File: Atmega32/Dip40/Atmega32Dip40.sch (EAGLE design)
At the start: 0 parts

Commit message: Add Atmega32 DIP40
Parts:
- added C1, C2: 100n, resistor:C-EUC1206
- added C10, C3: 22p, resistor:C-EUC1206
- added FTDI: 6H, adafruit:PINHD-1X6
- added IC1: MEGA32-P, atmel:MEGA32-P
- added L1: SMT, adafruit:LEDSMT1206
- added LED_ASP: BLUE_SMT, adafruit:LEDSMT1206
- added Q3: 16m, adafruit:CRYSTALHC49UP
- added R3: 330, resistor:R-EU_R1206
- added R4: 1k, resistor:R-EU_R1206
- added R5, R6: 10K, resistor:R-EU_0204/7
- added R7: 100K, resistor:R-EU_0204/7
- added X3: 057-010-1, con-panduit:057-010-1
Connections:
- new net DTR: C2.1, FTDI.1
- new net GND: C1.1, C10.1, C3.1, FTDI.6, IC1.GND, IC1.GND@1, L1.C, LED_ASP.C, X3-10.S, X3-3.S, X3-4.S, X3-6.S, X3-8.S
- new net LED_13: IC1.(OC1A)PD5, R3.1
- new net MISO: IC1.(MISO)PB6, X3-9.S
- new net MOSI: IC1.(MOSI)PB5, X3-1.S
- new net N$2: L1.A, R3.2
- new net N$3: LED_ASP.A, R4.2
- new net N$4: C1.2, IC1.AREF
- new net OX1: C10.2, IC1.XTAL2, Q3.2
- new net OX2: C3.2, IC1.XTAL1, Q3.1
- new net RESET: C2.2, FTDI.5, IC1.RESET, R7.1, X3-5.S
- new net RX: FTDI.2, IC1.(RXD)PD0
- new net SCK: IC1.(SCK)PB7, X3-7.S
- new net SCL: IC1.(SCL)PC0, R5.2
- new net SDA: IC1.(SDA)PC1, R6.2
- new net TX: FTDI.3, IC1.(TXD)PD1
- new net VCC: FTDI.4, IC1.AVCC, IC1.VCC, R4.1, R5.1, R6.1, R7.2, X3-2.S
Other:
- note added: "DTR"
- note added: "FTDI Serial"
- note added: "I2S Pull-UP"
- note added: "LED DIGITAL 13"
- note added: "Oscillator MCU"
- note added: "RESET"
- note added: "RX"
- note added: "SPI"
- note added: "TX"

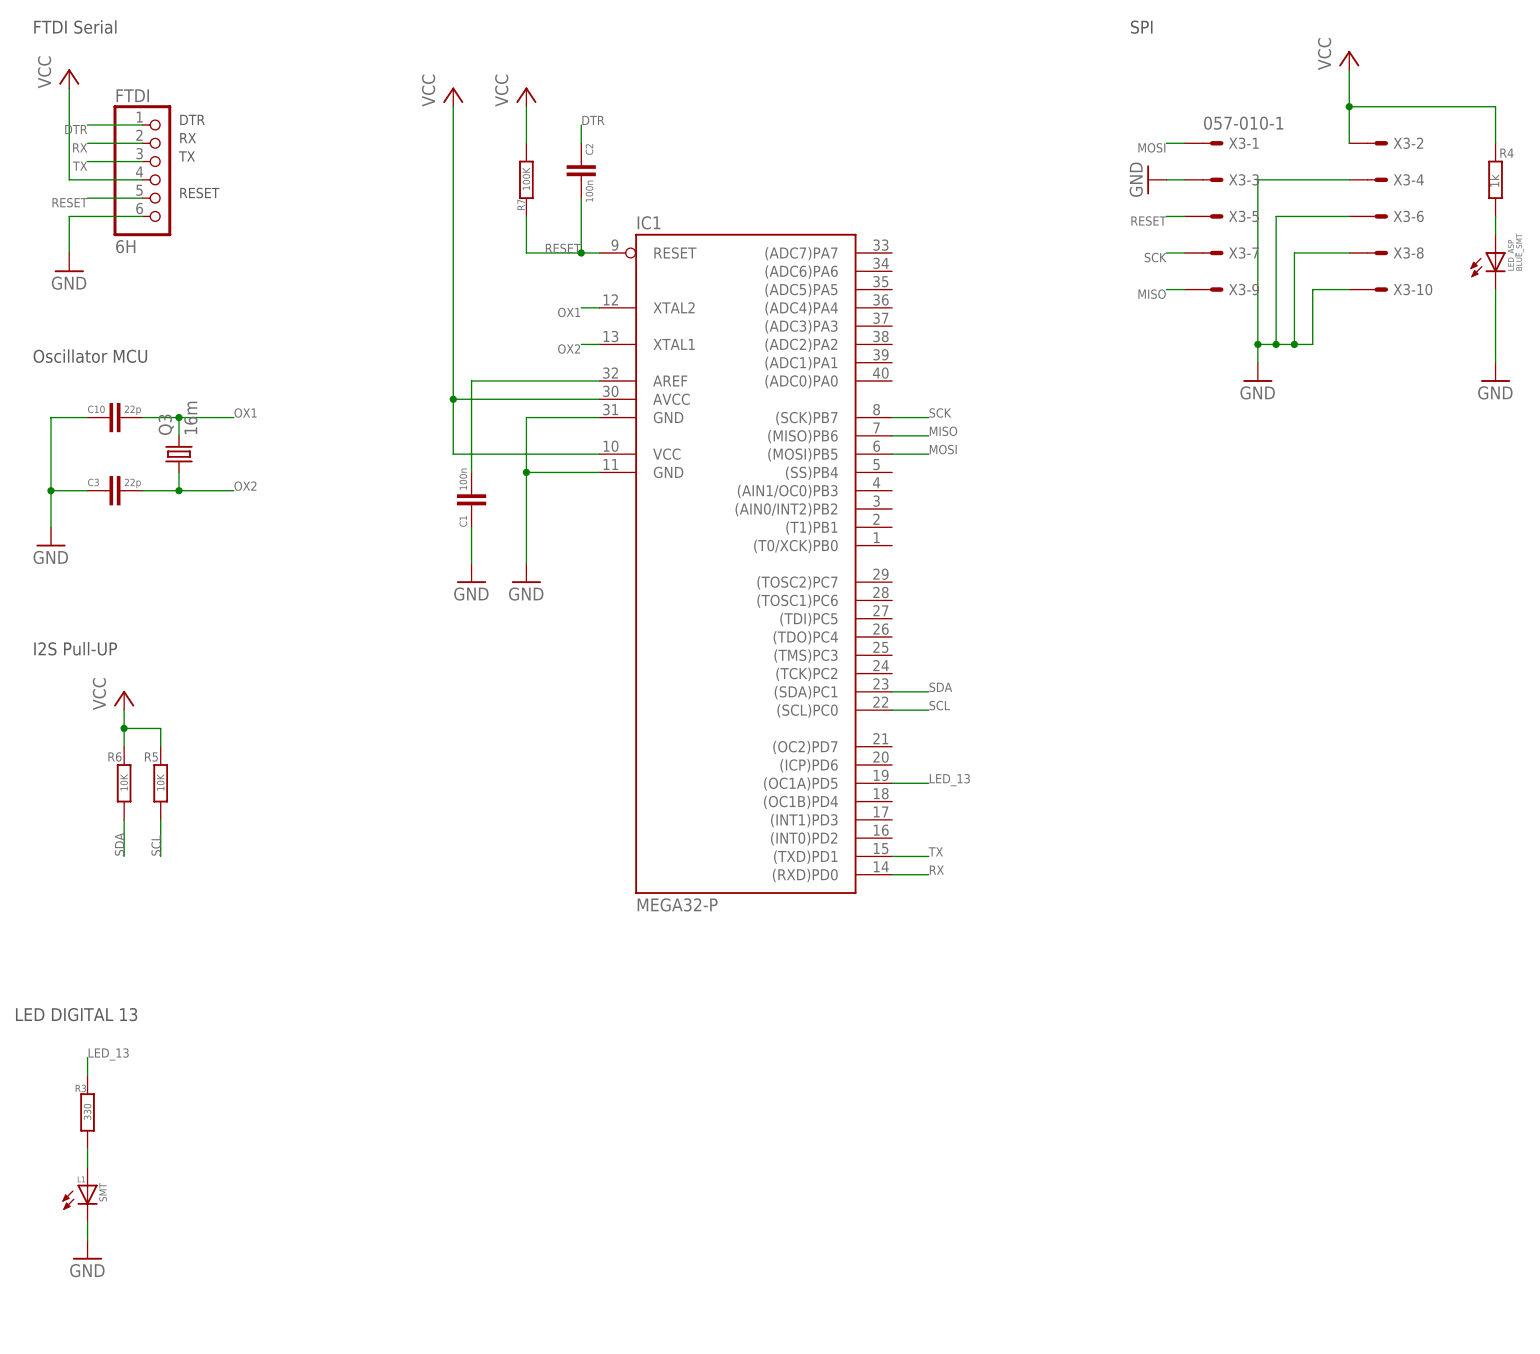
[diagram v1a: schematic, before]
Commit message: Update Atmega32 Dip 40
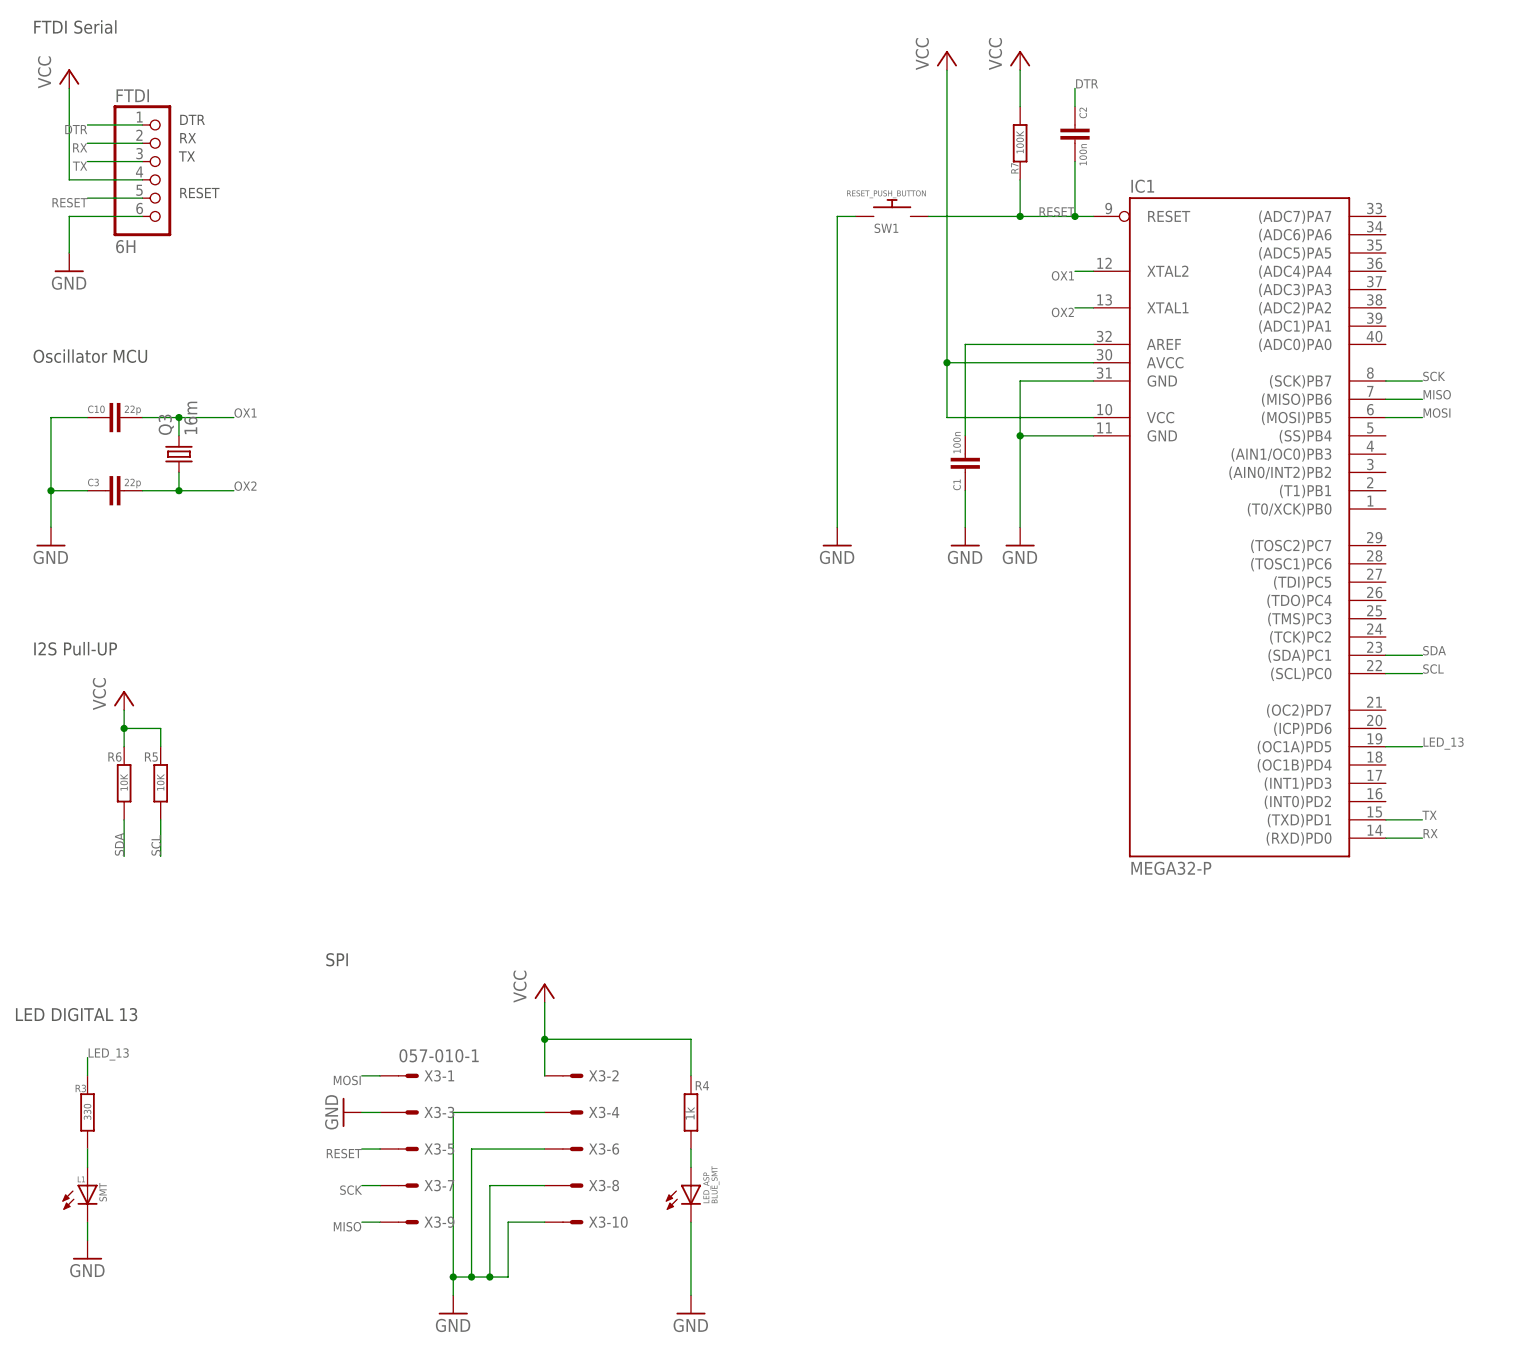
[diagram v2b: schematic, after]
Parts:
- added RESET_PUSH_BUTTON: SW1, adafruit:SWITCH_PUSHBUTTONEVQ-PE
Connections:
- net GND: now also RESET_PUSH_BUTTON.P$1
- net RESET: now also RESET_PUSH_BUTTON.P$2
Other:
- moved on the sheet: C1, C2, IC1, LED_ASP, R4, R7, X3-1, X3-10, X3-2, X3-3, X3-4, X3-5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

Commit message: update atmega32 dip 40
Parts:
- renumbered FTDI to PIN_SERIAL
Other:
- note added: "<< Mostly not used"
- note added: "I2C Pull-UP"
- note added: "USB Serial"
- note removed: "FTDI Serial"
- note removed: "I2S Pull-UP"
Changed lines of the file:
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@@
 <part name="LED_ASP" library="adafruit" deviceset="LED" device="SMT1206" value="BLUE_SMT"/>
 <part name="GND9" library="supply1" deviceset="GND" device=""/>
-<part name="FTDI" library="adafruit" deviceset="PINHD-1X6" device="" value="6H"/>
+<part name="PIN_SERIAL" library="adafruit" deviceset="PINHD-1X6" device="" value="6H"/>
 <part name="P+5" library="supply1" deviceset="VCC" device=""/>
 <part name="GND6" library="supply1" deviceset="GND" device=""/>
@@
 <text x="71.12" y="60.96" size="1.778" layer="97">SPI</text>
 <text x="30.48" y="144.78" size="1.778" layer="97">Oscillator MCU</text>
-<text x="30.48" y="190.5" size="1.778" layer="97">FTDI Serial</text>
+<text x="30.48" y="190.5" size="1.778" layer="97">USB Serial</text>
 <text x="50.8" y="177.8" size="1.4224" layer="97">DTR</text>
 <text x="50.8" y="175.26" size="1.4224" layer="97">RX</text>
 <text x="50.8" y="172.72" size="1.4224" layer="97">TX</text>
 <text x="50.8" y="167.64" size="1.4224" layer="97">RESET</text>
-<text x="30.48" y="104.14" size="1.778" layer="97">I2S Pull-UP</text>
+<text x="30.48" y="104.14" size="1.778" layer="97">I2C Pull-UP</text>
 <text x="27.94" y="53.34" size="1.778" layer="97">LED DIGITAL 13</text>
+<text x="60.96" y="167.64" size="1.778" layer="97">&lt;&lt; Mostly not used</text>
+<text x="60.96" y="177.8" size="1.778" layer="97">&lt;&lt; Mostly not used</text>
 </plain>
 <instances>
@@
 </instance>
 <instance part="GND9" gate="1" x="121.92" y="12.7"/>
-<instance part="FTDI" gate="A" x="48.26" y="170.18"/>
+<instance part="PIN_SERIAL" gate="A" x="48.26" y="170.18"/>
 <instance part="P+5" gate="VCC" x="35.56" y="185.42"/>
 <instance part="GND6" gate="1" x="35.56" y="157.48"/>
@@
 </segment>
 <segment>
-<pinref part="FTDI" gate="A" pin="6"/>
+<pinref part="PIN_SERIAL" gate="A" pin="6"/>
 <wire x1="45.72" y1="165.1" x2="35.56" y2="165.1" width="0.1524" layer="91"/>
 <pinref part="GND6" gate="1" pin="GND"/>
@@
 </segment>
 <segment>
-<pinref part="FTDI" gate="A" pin="4"/>
+<pinref part="PIN_SERIAL" gate="A" pin="4"/>
 <wire x1="45.72" y1="170.18" x2="35.56" y2="170.18" width="0.1524" layer="91"/>
 <pinref part="P+5" gate="VCC" pin="VCC"/>
@@
 </segment>
 <segment>
-<pinref part="FTDI" gate="A" pin="5"/>
+<pinref part="PIN_SERIAL" gate="A" pin="5"/>
 <wire x1="45.72" y1="167.64" x2="38.1" y2="167.64" width="0.1524" layer="91"/>
 <label x="38.1" y="167.64" size="1.27" layer="95" font="vector" rot="R180"/>
@@
 </segment>
 <segment>
-<pinref part="FTDI" gate="A" pin="1"/>
+<pinref part="PIN_SERIAL" gate="A" pin="1"/>
 <wire x1="45.72" y1="177.8" x2="38.1" y2="177.8" width="0.1524" layer="91"/>
 <label x="38.1" y="177.8" size="1.27" layer="95" font="vector" rot="R180"/>
@@
 </segment>
 <segment>
-<pinref part="FTDI" gate="A" pin="3"/>
+<pinref part="PIN_SERIAL" gate="A" pin="3"/>
 <wire x1="45.72" y1="172.72" x2="38.1" y2="172.72" width="0.1524" layer="91"/>
 <label x="38.1" y="172.72" size="1.27" layer="95" font="vector" rot="R180"/>
@@
 </segment>
 <segment>
-<pinref part="FTDI" gate="A" pin="2"/>
+<pinref part="PIN_SERIAL" gate="A" pin="2"/>
 <wire x1="45.72" y1="175.26" x2="38.1" y2="175.26" width="0.1524" layer="91"/>
 <label x="38.1" y="175.26" size="1.27" layer="95" font="vector" rot="R180"/>
